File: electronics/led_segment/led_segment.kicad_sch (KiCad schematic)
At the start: 11 parts, among them J1 RJ45, J2 RJ45, J3 Conn_01x04, J4 Screw_Terminal_01x02, J5 Screw_Terminal_01x02, U3 LP2950-5.0_TO252

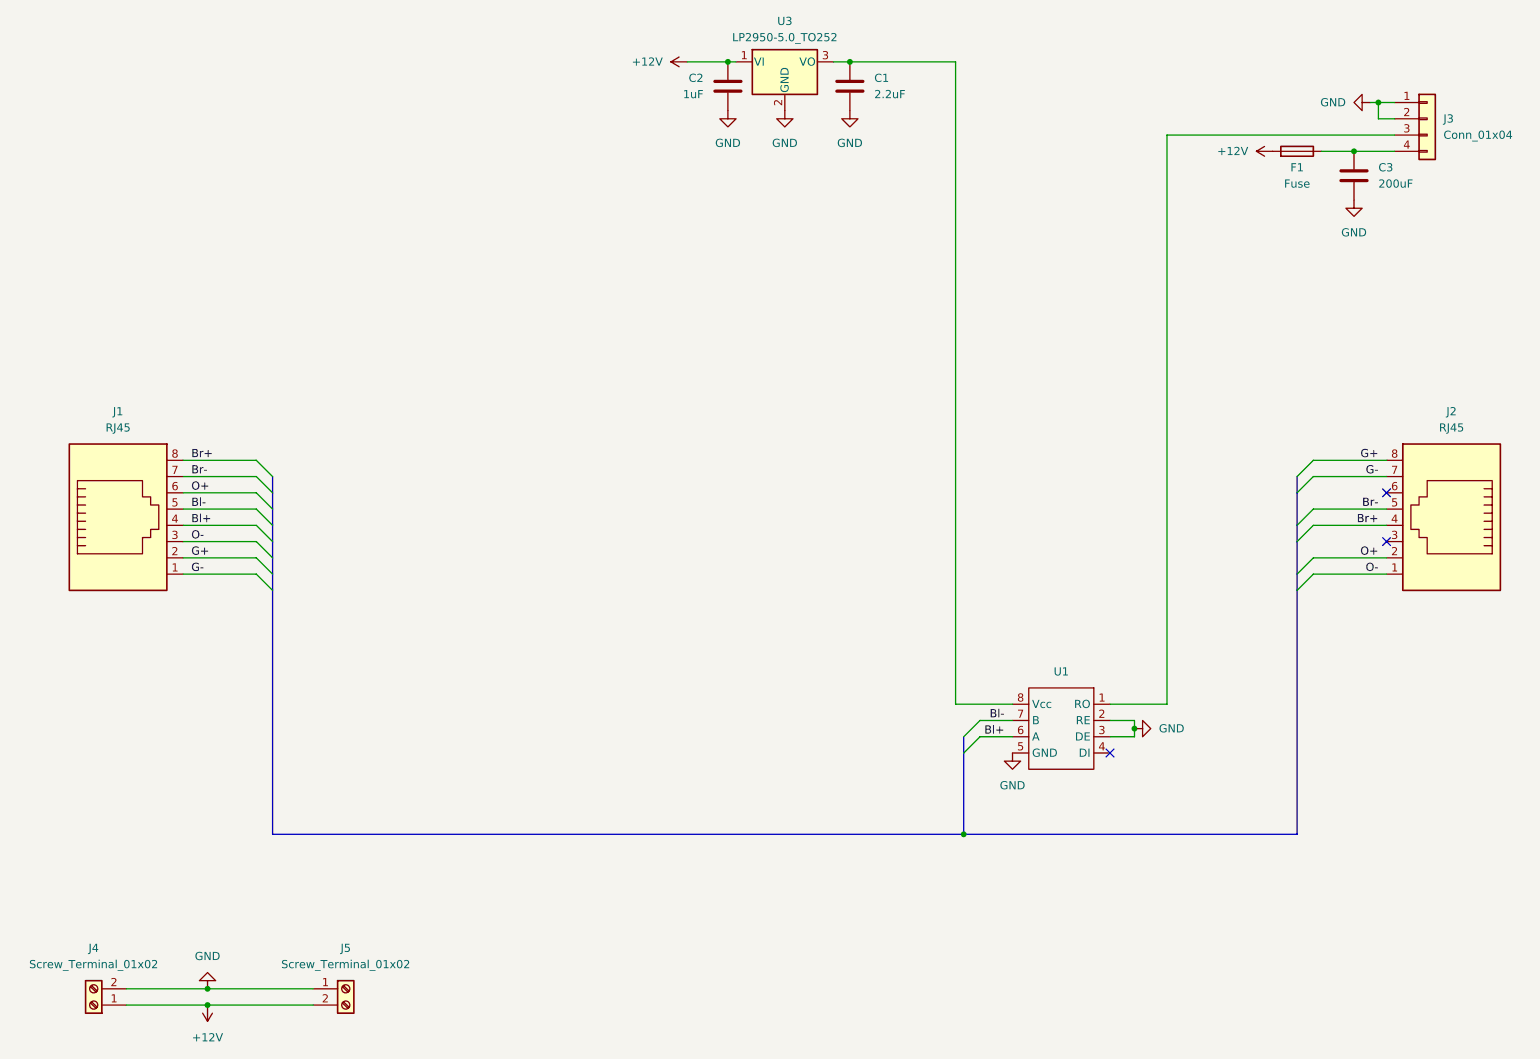
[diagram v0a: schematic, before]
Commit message: re-implement jumpers
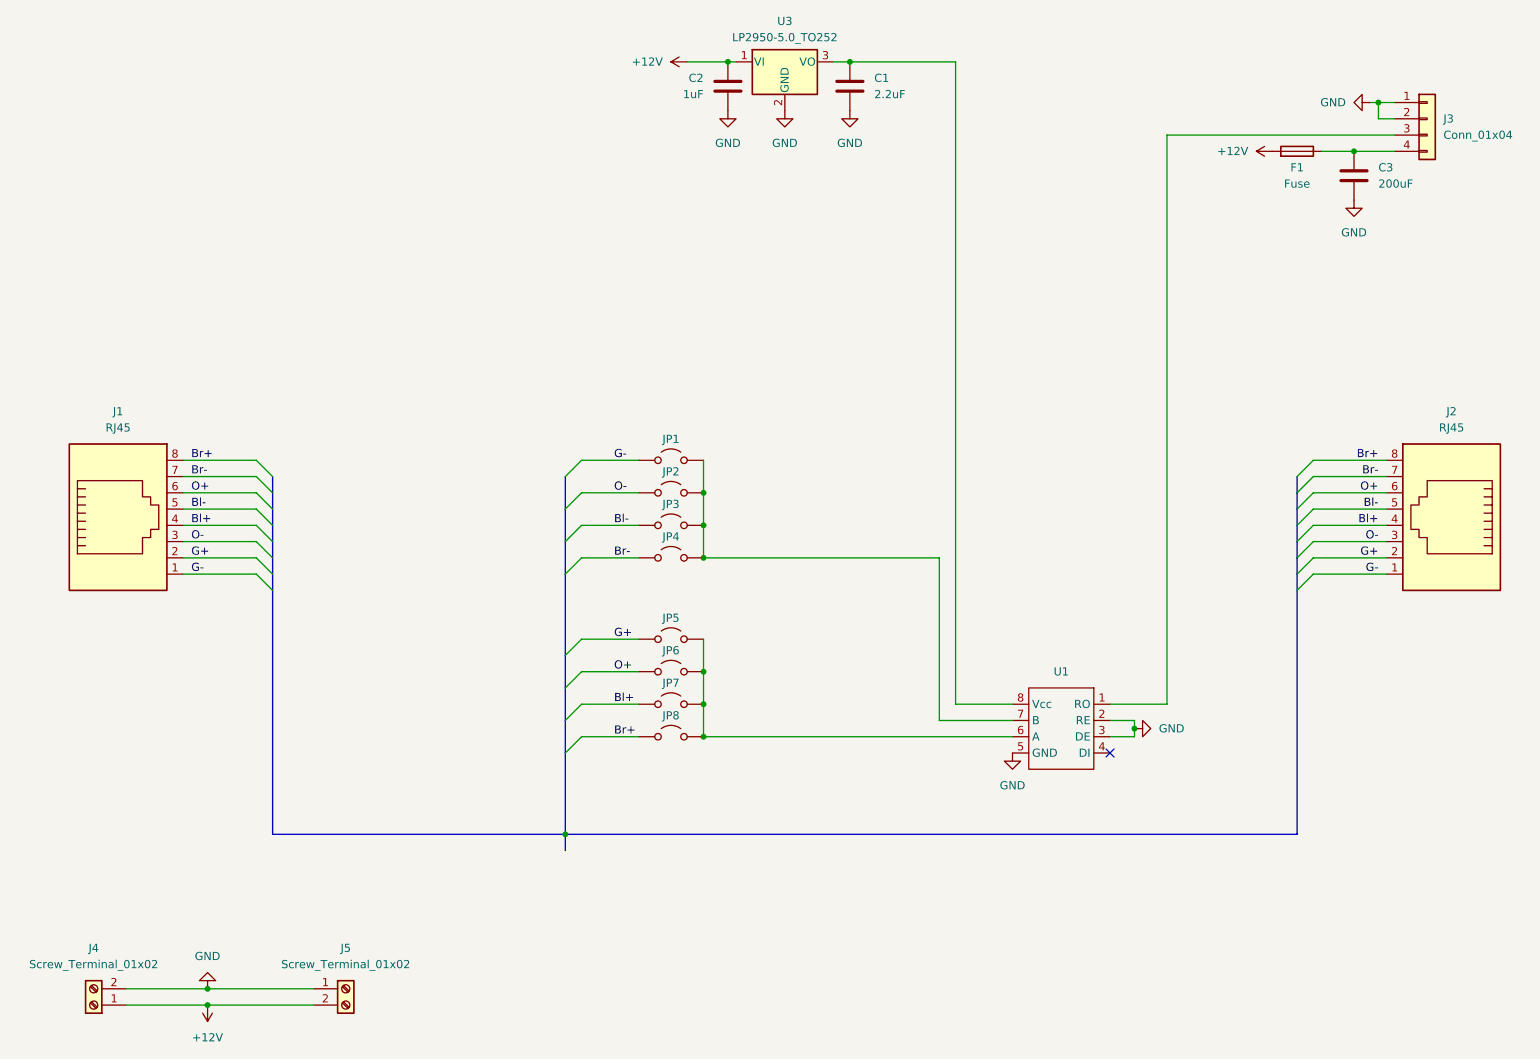
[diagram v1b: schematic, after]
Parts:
- added JP1, JP2, JP3, JP4, JP5, JP6, JP7, JP8: Jumper_2_Open, Jumper:SolderJumper-2_P1.3mm_Open_Pad1.0x1.5mm, symbol Jumper:Jumper_2_Open
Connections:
- net Bl+: now also J2.4, JP7.1 (A); no longer U1.6 (A)
- net Bl-: now also J2.5, JP3.1 (A); no longer U1.7 (B)
- net Br+: now also J2.8, JP8.1 (A); no longer J2.4
- net Br-: now also J2.7, JP4.1 (A); no longer J2.5
- net G+: now also J2.2, JP5.1 (A); no longer J2.8
- net G-: now also J2.1, JP1.1 (A); no longer J2.7
- net O+: now also J2.6, JP6.1 (A); no longer J2.2
- net O-: now also J2.3, JP2.1 (A); no longer J2.1
- new net: JP5.2 (B), JP6.2 (B), JP7.2 (B), JP8.2 (B), U1.6 (A)
- new net: JP1.2 (B), JP2.2 (B), JP3.2 (B), JP4.2 (B), U1.7 (B)
- no-connect marks 3 -> 1

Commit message: get peer review on rev.3 of boards
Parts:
- added D1: LED, LED_THT:LED_D3.0mm, symbol Device:LED
- added JP9: Jumper_2_Open, Jumper:SolderJumper-2_P1.3mm_Open_Pad1.0x1.5mm, symbol Jumper:Jumper_2_Open
- added R1: R, Resistor_SMD:R_1206_3216Metric, symbol Device:R
- added R2: 120, Resistor_SMD:R_1206_3216Metric, symbol Device:R
- J1, J2: footprint SMM:RC01516 -> Connector_RJ:RJ45_Ninigi_GE
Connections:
- net GND: now also D1.1 (K); no longer J3.2 (Pin_2)
- net at J3.3 (Pin_3), U1.1 (RO): now also JP9.1 (A)
- net at JP5.2 (B), JP6.2 (B), JP7.2 (B)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: now also R1.2
- net at JP1.2 (B), JP2.2 (B), JP3.2 (B)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: now also R1.1
- net at C1.1, U1.8 (Vcc), U3.3 (VO): now also R2.1
- new net: D1.2 (A), R2.2
- new net: J3.2 (Pin_2), JP9.2 (B)
